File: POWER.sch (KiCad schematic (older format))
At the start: 39 parts, among them J6001 BATT1, J6002 BATT2_XT60, J6003 BATT2_JST, J6004 BATT4_CELL2, J6005 BATT4_CELL1, J6007 BATT5_CELL1, J6008 BATT3_JST, U6001 D24V50F5, U6002 D36V28F3, U6003 LM7809_TO220, U6004 D36V50F6, U6005 D36V50F6, U6006 D24V50F5

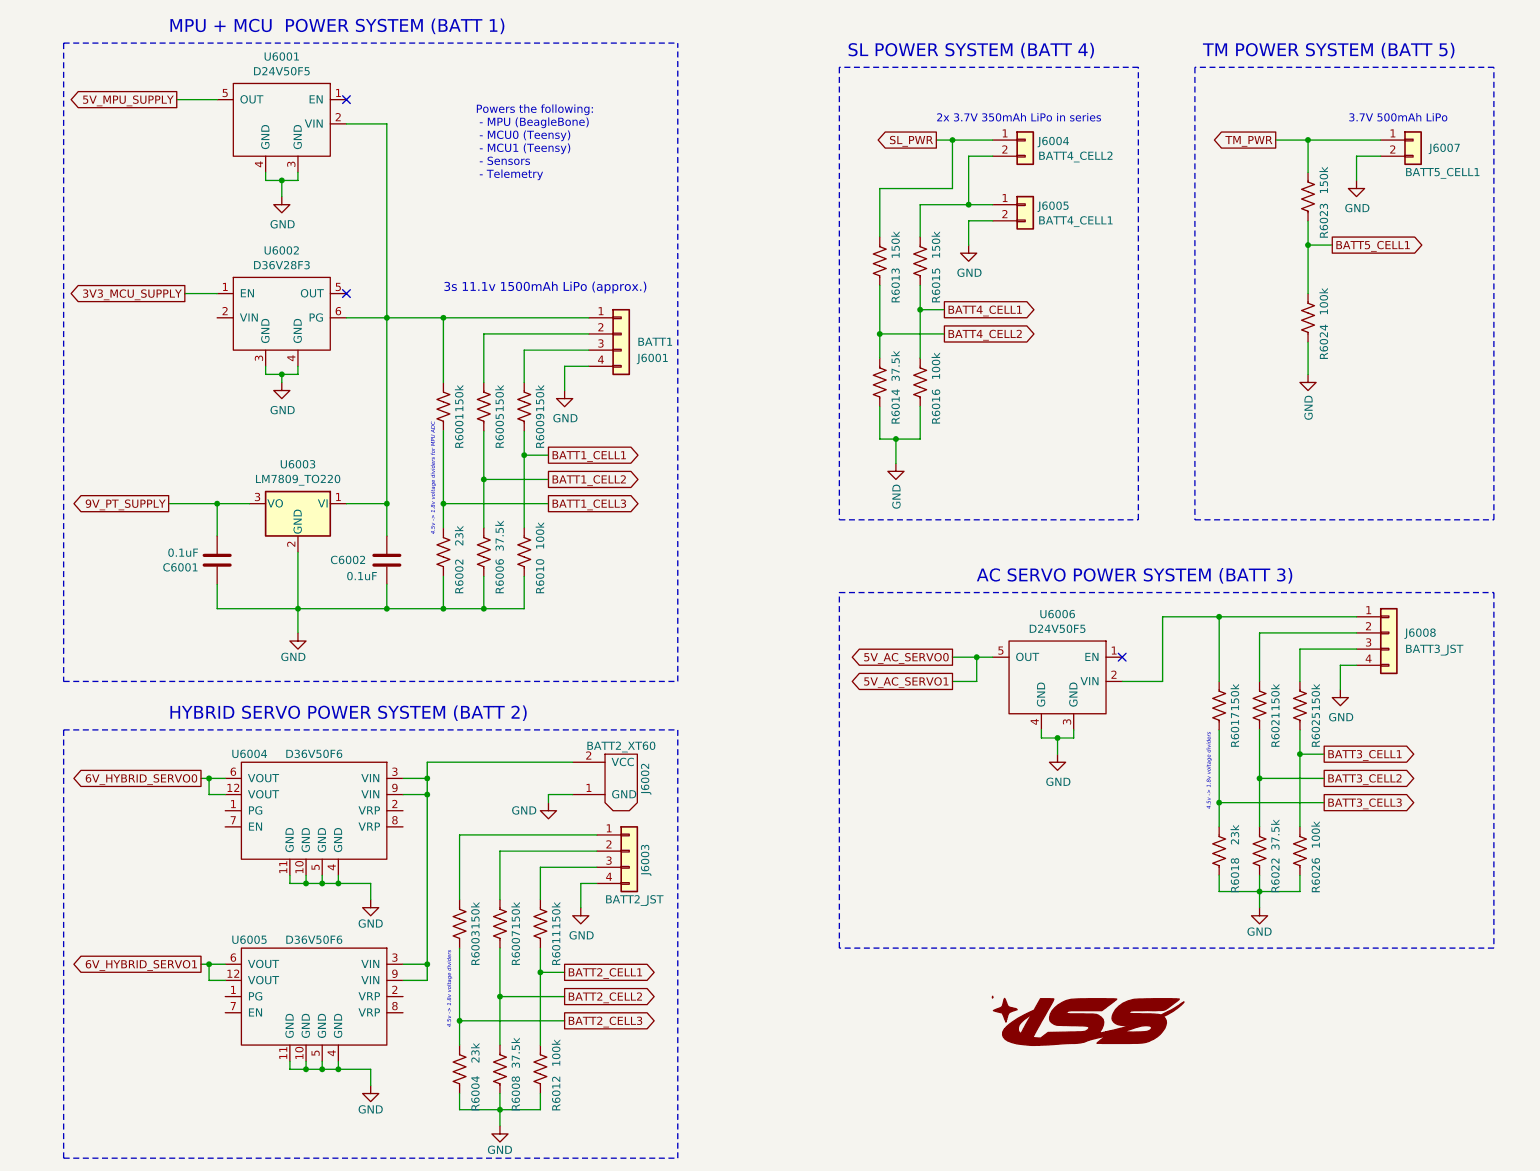
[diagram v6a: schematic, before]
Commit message: Made symbols/footprints for locking Molex connectors
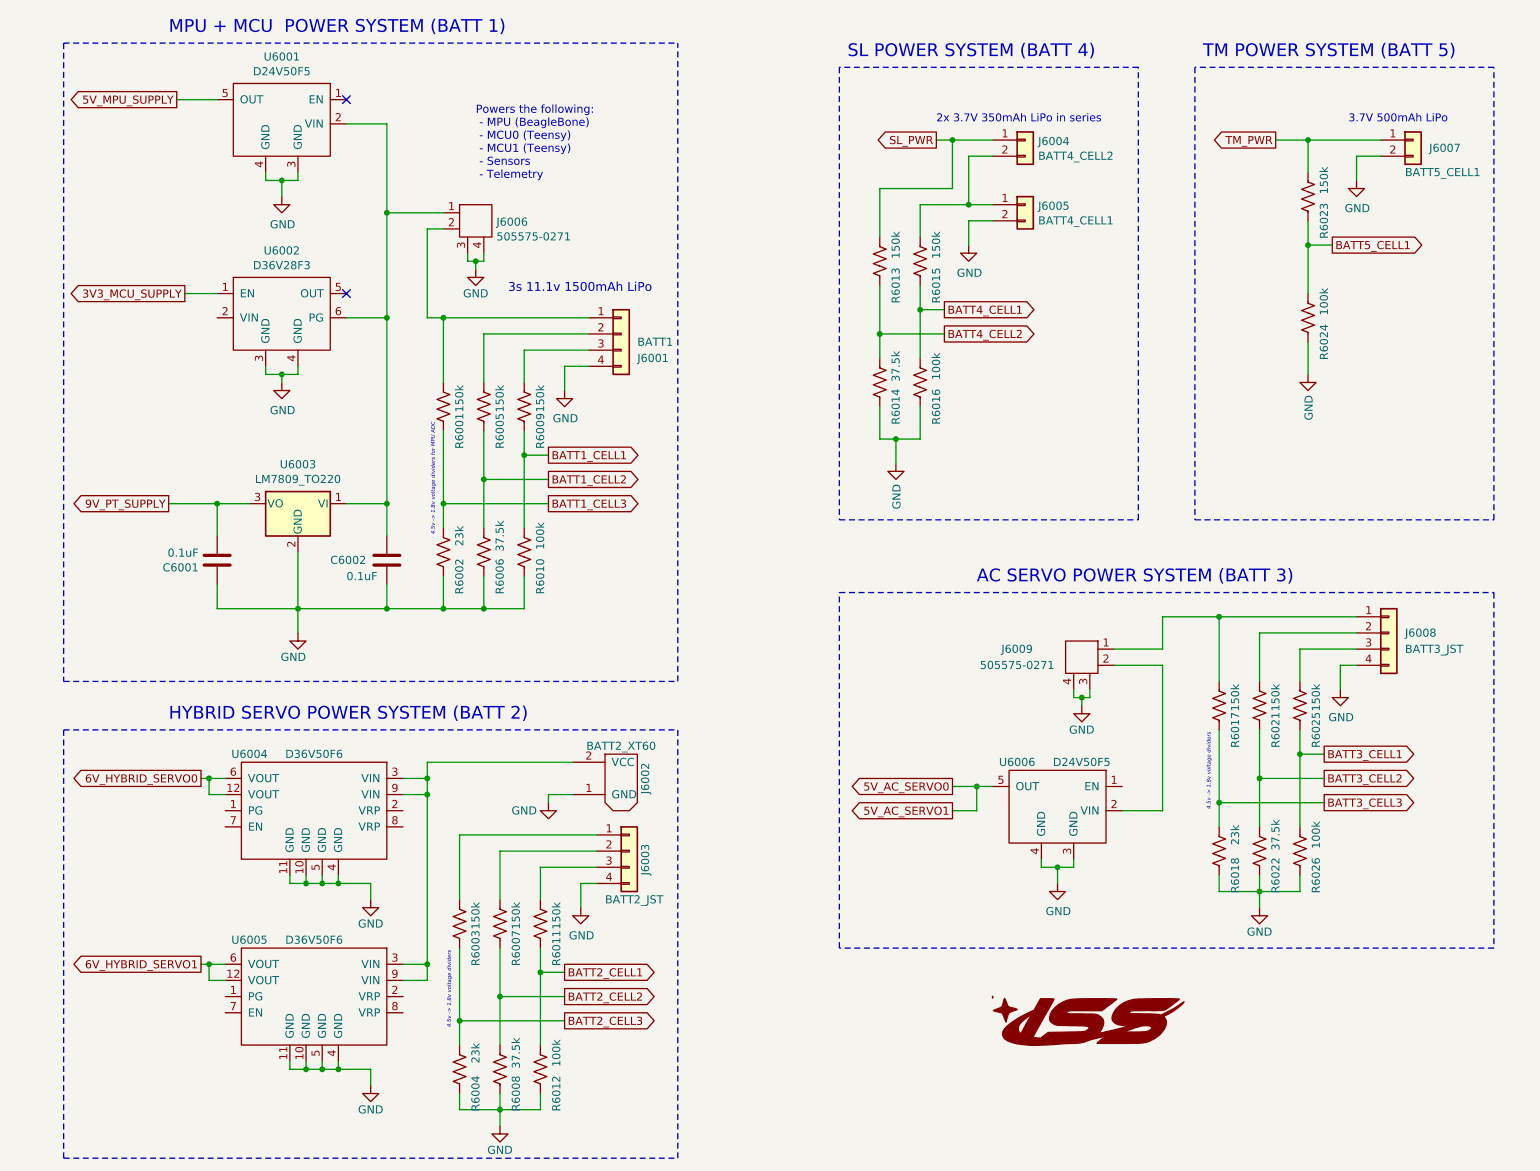
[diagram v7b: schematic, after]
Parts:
- added J6006, J6009: 505575-0271, 505575-0271:505575-0271, symbol 505575-0271:505575-0271
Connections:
- net GND: now also J6006.3, J6006.4, J6009.3, J6009.4
- net at C6002.1, U6001.2 (VIN), U6002.6 (PG)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: now also J6006.1; no longer J6001.1 (Pin_1), R6001.2
- net at J6008.1 (Pin_1), R6017.2: now also J6009.1; no longer U6006.2 (VIN)
- new net: J6001.1 (Pin_1), J6006.2, R6001.2
- new net: J6009.2, U6006.2 (VIN)
- no-connect marks 3 -> 2
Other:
- note added: "3s 11.1v 1500mAh LiPo"
- note removed: "3s 11.1v 1500mAh LiPo (approx.)"
- moved on the sheet: U6006
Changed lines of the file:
@@
 L D24V50F5:D24V50F5 U6006
 U 1 1 5FE7A4D8
-P 7400 4400
-F 0 "U6006" H 7400 4515 50  0000 C CNN
-F 1 "D24V50F5" H 7400 4424 50  0000 C CNN
-F 2 "D24V50F5:D24V50F5" H 7400 4400 50  0001 C CNN
-F 3 "" H 7400 4400 50  0001 C CNN
-	1    7400 4400
+P 7400 5200
+F 0 "U6006" H 7650 5200 50  0000 C CNN
+F 1 "D24V50F5" H 7250 5200 50  0000 C CNN
+F 2 "D24V50F5:D24V50F5" H 7400 5200 50  0001 C CNN
+F 3 "" H 7400 5200 50  0001 C CNN
+	1    7400 5200
 	-1   0    0    -1
 $EndComp
@@
 L power:GND #PWR06012
 U 1 1 5FE7A4DE
-P 7400 5150
-F 0 "#PWR06012" H 7400 4900 50  0001 C CNN
-F 1 "GND" H 7405 4977 50  0000 C CNN
-F 2 "" H 7400 5150 50  0001 C CNN
-F 3 "" H 7400 5150 50  0001 C CNN
-	1    7400 5150
-	1    0    0    -1
-$EndComp
-Wire Wire Line
-	7300 5000 7300 5050
-Wire Wire Line
-	7300 5050 7400 5050
-Wire Wire Line
-	7400 5050 7400 5150
-Wire Wire Line
-	7500 5000 7500 5050
-Wire Wire Line
-	7500 5050 7400 5050
-Connection ~ 7400 5050
-NoConn ~ 7800 4550
-Text GLabel 6750 4550 0    50   Output ~ 0
+P 7400 5950
+F 0 "#PWR06012" H 7400 5700 50  0001 C CNN
+F 1 "GND" H 7405 5777 50  0000 C CNN
+F 2 "" H 7400 5950 50  0001 C CNN
+F 3 "" H 7400 5950 50  0001 C CNN
+	1    7400 5950
+	1    0    0    -1
+$EndComp
+Wire Wire Line
+	7300 5800 7300 5850
+Wire Wire Line
+	7300 5850 7400 5850
+Wire Wire Line
+	7400 5850 7400 5950
+Wire Wire Line
+	7500 5800 7500 5850
+Wire Wire Line
+	7500 5850 7400 5850
+Connection ~ 7400 5850
+Text GLabel 6750 5350 0    50   Output ~ 0
 5V_AC_SERVO0
 Wire Wire Line
-	7000 4550 6900 4550
-Text GLabel 6750 4700 0    50   Output ~ 0
+	7000 5350 6900 5350
+Text GLabel 6750 5500 0    50   Output ~ 0
 5V_AC_SERVO1
 Wire Wire Line
-	6750 4700 6900 4700
-Wire Wire Line
-	6900 4700 6900 4550
-Connection ~ 6900 4550
-Wire Wire Line
-	6900 4550 6750 4550
+	6750 5500 6900 5500
+Wire Wire Line
+	6900 5500 6900 5350
+Connection ~ 6900 5350
+Wire Wire Line
+	6900 5350 6750 5350
 Wire Wire Line
 	9050 5450 8400 5450
@@
 Connection ~ 8400 4300
 Wire Wire Line
-	8050 4300 8050 4700
-Wire Wire Line
-	8050 4700 7800 4700
-Wire Wire Line
 	8050 4300 8400 4300
 Wire Notes Line
@@
 	1250 750  1250 4700
 Wire Wire Line
-	3250 1250 3250 2450
+	3250 1250 3250 1800
 Wire Wire Line
 	4200 6950 4200 6500
@@
 	-1   0    0    -1
 $EndComp
-Text Notes 3600 2300 0    55   ~ 0
-3s 11.1v 1500mAh LiPo (approx.)
-Wire Wire Line
-	3250 2450 3600 2450
+Text Notes 4000 2300 0    55   ~ 0
+3s 11.1v 1500mAh LiPo
 Wire Wire Line
 	3600 2450 4500 2450
-Connection ~ 3600 2450
 Wire Wire Line
 	3600 2850 3600 2450
@@
 Wire Wire Line
 	8750 1350 8950 1350
+$Comp
+L 505575-0271:505575-0271 J6009
+U 1 1 5FABA8F9
+P 7550 4450
+F 0 "J6009" H 7950 4400 50  0000 C CNN
+F 1 "505575-0271" H 7950 4300 50  0000 C CNN
+F 2 "505575-0271:505575-0271" H 8200 4350 50  0001 C CNN
+F 3 "" H 7550 4450 50  0001 C CNN
+	1    7550 4450
+	-1   0    0    -1
+$EndComp
+Wire Wire Line
+	8050 4300 8050 4500
+Wire Wire Line
+	8050 4500 7750 4500
+Wire Wire Line
+	7750 4600 8050 4600
+Wire Wire Line
+	8050 4600 8050 5500
+Wire Wire Line
+	8050 5500 7800 5500
+Wire Wire Line
+	7500 4750 7500 4800
+Wire Wire Line
+	7500 4800 7550 4800
+Wire Wire Line
+	7600 4800 7600 4750
+Wire Wire Line
+	7550 4800 7550 4850
+Connection ~ 7550 4800
+Wire Wire Line
+	7550 4800 7600 4800
+$Comp
+L power:GND #PWR0103
+U 1 1 5FAF2FF3
+P 7550 4850
+F 0 "#PWR0103" H 7550 4600 50  0001 C CNN
+F 1 "GND" H 7550 4700 50  0000 C CNN
+F 2 "" H 7550 4850 50  0001 C CNN
+F 3 "" H 7550 4850 50  0001 C CNN
+	1    7550 4850
+	1    0    0    -1
+$EndComp
+$Comp
+L 505575-0271:505575-0271 J6006
+U 1 1 5FB0BCE9
+P 3800 1750
+F 0 "J6006" H 3928 1643 50  0000 L CNN
+F 1 "505575-0271" H 3928 1552 50  0000 L CNN
+F 2 "505575-0271:505575-0271" H 4450 1650 50  0001 C CNN
+F 3 "" H 3800 1750 50  0001 C CNN
+	1    3800 1750
+	1    0    0    -1
+$EndComp
+Wire Wire Line
+	3600 2450 3500 2450
+Wire Wire Line
+	3500 1900 3600 1900
+Connection ~ 3600 2450
+Wire Wire Line
+	3600 1800 3250 1800
+Wire Wire Line
+	3750 2050 3750 2100
+Wire Wire Line
+	3750 2100 3800 2100
+Wire Wire Line
+	3850 2100 3850 2050
+Wire Wire Line
+	3800 2100 3800 2150
+$Comp
+L power:GND #PWR0104
+U 1 1 5FB3E1CE
+P 3800 2150
+F 0 "#PWR0104" H 3800 1900 50  0001 C CNN
+F 1 "GND" H 3800 2000 50  0000 C CNN
+F 2 "" H 3800 2150 50  0001 C CNN
+F 3 "" H 3800 2150 50  0001 C CNN
+	1    3800 2150
+	1    0    0    -1
+$EndComp
+Connection ~ 3250 1800
+Wire Wire Line
+	3250 1800 3250 2450
+Connection ~ 3800 2100
+Wire Wire Line
+	3800 2100 3850 2100
+Wire Wire Line
+	3500 1900 3500 2450
 $EndSCHEMATC

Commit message: electrical connections, added 3rd active control servo, added footprints for hybrid regulators
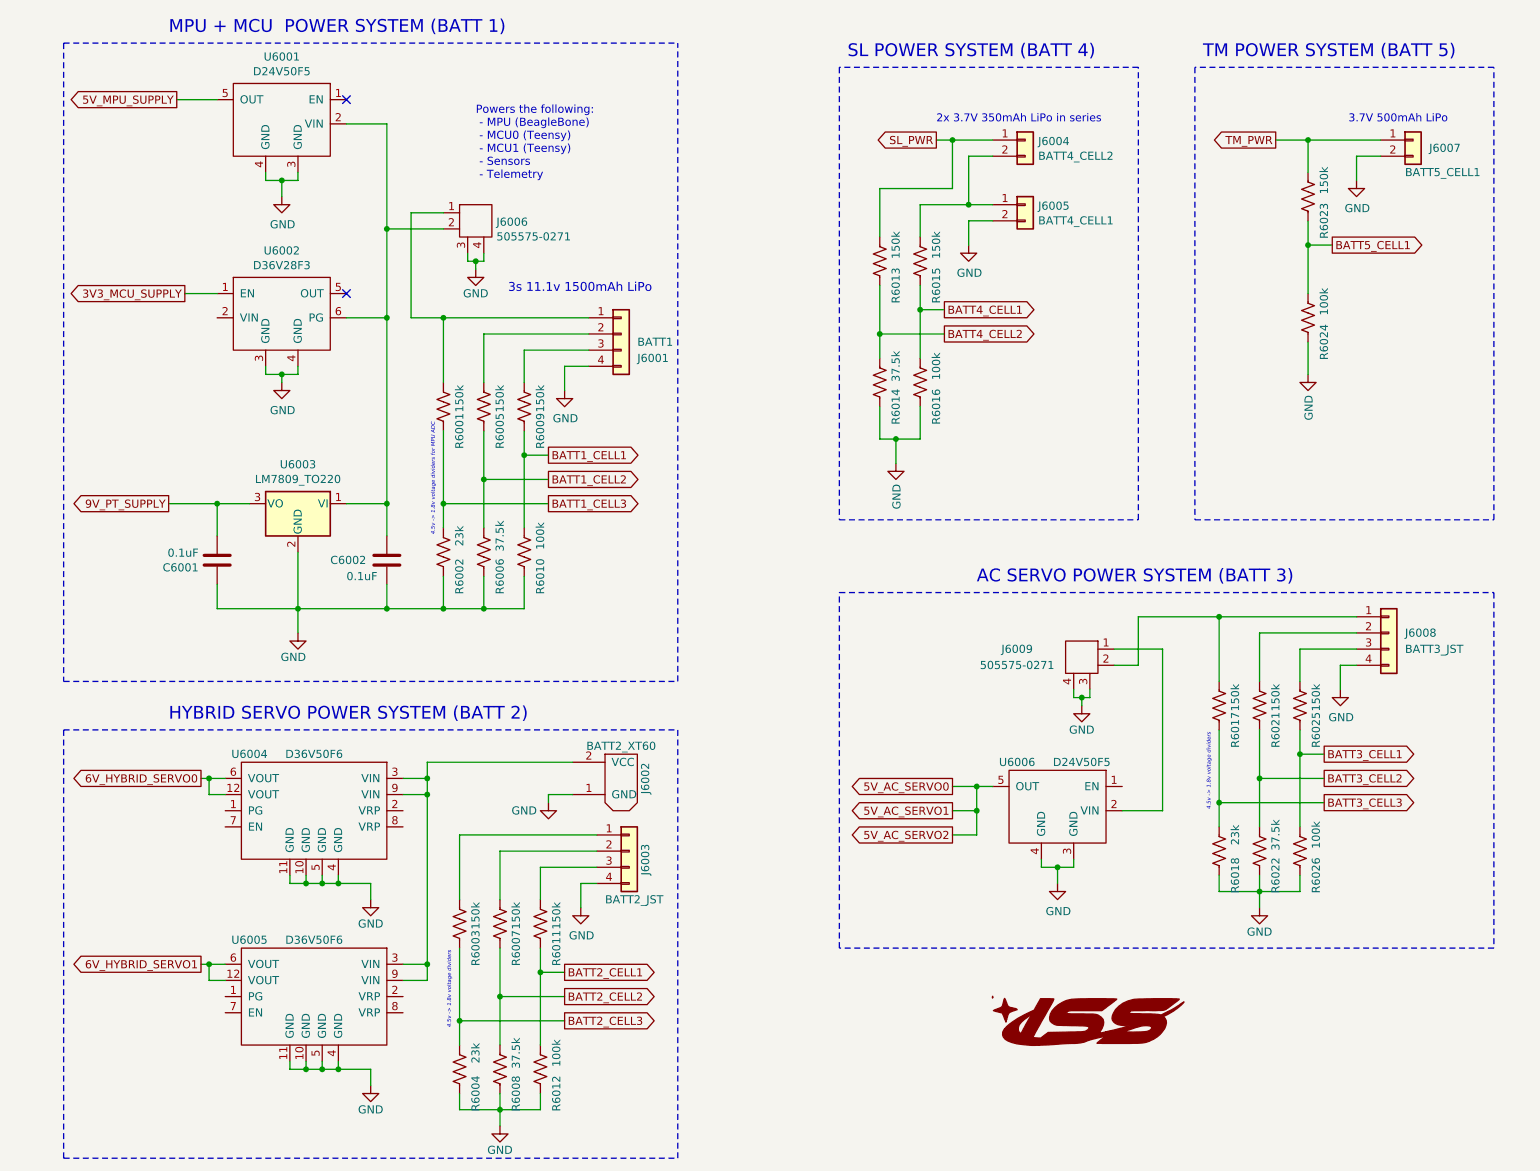
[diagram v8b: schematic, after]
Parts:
- U6004, U6005: footprint D36V50F6:D36V50F6 -> D36V50F6:D36V50F6-TARS
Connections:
- net at J6001.1 (Pin_1), R6001.2: now also J6006.1; no longer J6006.2
- net at C6002.1, U6001.2 (VIN), U6002.6 (PG)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: now also J6006.2; no longer J6006.1
- net at J6008.1 (Pin_1), R6017.2: now also J6009.2; no longer J6009.1
- net at U6006.2 (VIN): now also J6009.1; no longer J6009.2
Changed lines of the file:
@@
 Wire Wire Line
 	8650 6000 8650 6100
-Connection ~ 8400 4300
-Wire Wire Line
-	8050 4300 8400 4300
 Wire Notes Line
 	5050 5000 5050 7650
@@
 Wire Notes Line
 	1250 750  1250 4700
-Wire Wire Line
-	3250 1250 3250 1800
 Wire Wire Line
 	4200 6950 4200 6500
@@
 Text GLabel 2100 5300 0    50   Output ~ 0
 6V_HYBRID_SERVO0
-$Comp
-L D36V50F6:D36V50F6 U6004
-U 1 1 5FAA681E
-P 2800 5150
-F 0 "U6004" H 3200 5150 50  0000 C CNN
-F 1 "D36V50F6" H 2800 5150 50  0000 C CNN
-F 2 "D36V50F6:D36V50F6" H 2800 5150 50  0001 C CNN
-F 3 "" H 2800 5150 50  0001 C CNN
-	1    2800 5150
-	-1   0    0    -1
-$EndComp
 Text GLabel 2100 6450 0    50   Output ~ 0
 6V_HYBRID_SERVO1
-$Comp
-L D36V50F6:D36V50F6 U6005
-U 1 1 5FACF193
-P 2800 6300
-F 0 "U6005" H 3200 6300 50  0000 C CNN
-F 1 "D36V50F6" H 2800 6300 50  0000 C CNN
-F 2 "D36V50F6:D36V50F6" H 2800 6300 50  0001 C CNN
-F 3 "" H 2800 6300 50  0001 C CNN
-	1    2800 6300
-	-1   0    0    -1
-$EndComp
 $Comp
 L Connector_Generic:Conn_01x04 J6003
@@
 $EndComp
 Wire Wire Line
-	8050 4300 8050 4500
-Wire Wire Line
-	8050 4500 7750 4500
-Wire Wire Line
-	7750 4600 8050 4600
-Wire Wire Line
-	8050 4600 8050 5500
-Wire Wire Line
-	8050 5500 7800 5500
-Wire Wire Line
 	7500 4750 7500 4800
 Wire Wire Line
@@
 $EndComp
 Wire Wire Line
-	3600 2450 3500 2450
-Wire Wire Line
-	3500 1900 3600 1900
-Connection ~ 3600 2450
-Wire Wire Line
-	3600 1800 3250 1800
-Wire Wire Line
 	3750 2050 3750 2100
 Wire Wire Line
@@
 	1    0    0    -1
 $EndComp
-Connection ~ 3250 1800
-Wire Wire Line
-	3250 1800 3250 2450
 Connection ~ 3800 2100
 Wire Wire Line
 	3800 2100 3850 2100
-Wire Wire Line
-	3500 1900 3500 2450
+Text GLabel 6750 5650 0    50   Output ~ 0
+5V_AC_SERVO2
+Wire Wire Line
+	6900 5500 6900 5650
+Wire Wire Line
+	6900 5650 6750 5650
+Connection ~ 6900 5500
+$Comp
+L D36V50F6:D36V50F6 U6005
+U 1 1 5FACF193
+P 2800 6300
+F 0 "U6005" H 3200 6300 50  0000 C CNN
+F 1 "D36V50F6" H 2800 6300 50  0000 C CNN
+F 2 "D36V50F6:D36V50F6-TARS" H 2800 6300 50  0001 C CNN
+F 3 "" H 2800 6300 50  0001 C CNN
+	1    2800 6300
+	-1   0    0    -1
+$EndComp
+$Comp
+L D36V50F6:D36V50F6 U6004
+U 1 1 5FAA681E
+P 2800 5150
+F 0 "U6004" H 3200 5150 50  0000 C CNN
+F 1 "D36V50F6" H 2800 5150 50  0000 C CNN
+F 2 "D36V50F6:D36V50F6-TARS" H 2800 5150 50  0001 C CNN
+F 3 "" H 2800 5150 50  0001 C CNN
+	1    2800 5150
+	-1   0    0    -1
+$EndComp
+Connection ~ 3600 2450
+Wire Wire Line
+	8050 5500 7800 5500
+Wire Wire Line
+	8050 4500 7750 4500
+Wire Wire Line
+	8050 4500 8050 5500
+Wire Wire Line
+	8400 4300 7900 4300
+Wire Wire Line
+	7900 4300 7900 4600
+Wire Wire Line
+	7900 4600 7750 4600
+Connection ~ 8400 4300
+Wire Wire Line
+	3400 2450 3400 1800
+Wire Wire Line
+	3400 2450 3600 2450
+Wire Wire Line
+	3400 1800 3600 1800
+Wire Wire Line
+	3250 1250 3250 1900
+Wire Wire Line
+	3600 1900 3250 1900
+Connection ~ 3250 1900
+Wire Wire Line
+	3250 1900 3250 2450
 $EndSCHEMATC
